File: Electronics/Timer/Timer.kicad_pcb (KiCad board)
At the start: 2 copper layers, 120 x 46 mm, 21 parts, among them J1 RJ12-UNSHLD, U1 74HC165, U2 MIC5504-3.3YM5

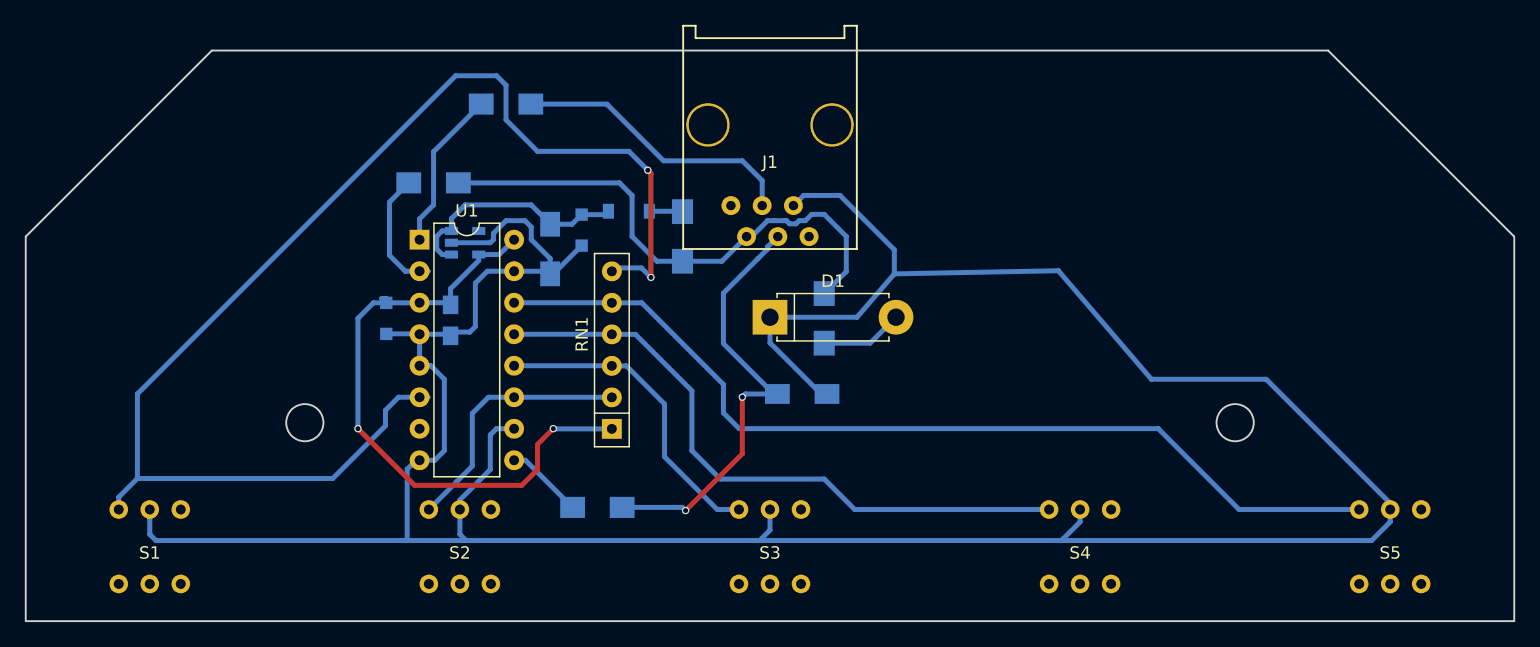
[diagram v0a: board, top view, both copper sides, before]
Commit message: Synchronized PCB with new netlist; cleaned up glitches.
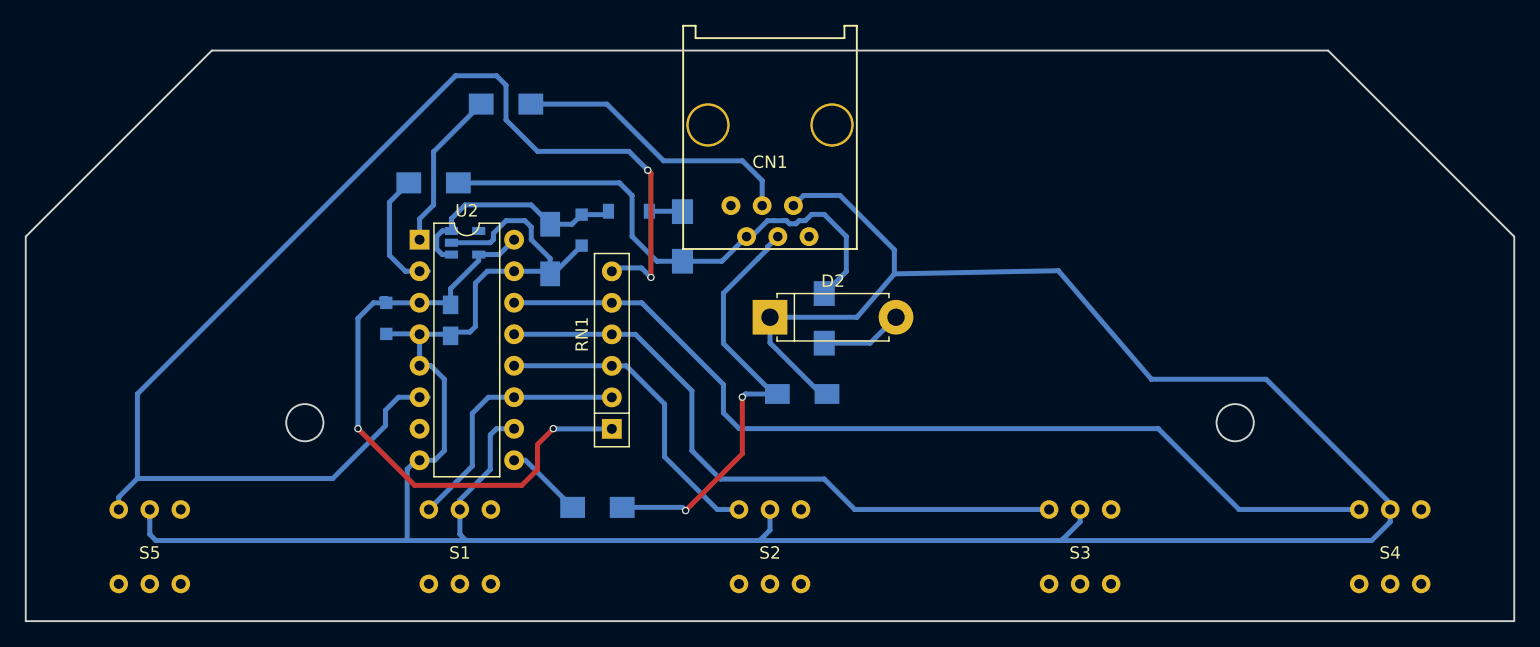
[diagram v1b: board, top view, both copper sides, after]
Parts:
- D1: renamed from D3; value D_Schottky -> BAT54
- D3: renamed from D2; value D_Zener_5V -> 5V
- D4: value D_Zener_3.3V -> 3.3V
- RN1: value R_Network05 -> 5x 47k
- turned C2 to 90 degrees
- turned R4 to 0 degrees
- renumbered C2 to C1, C1 to C2, J1 to CN1, D1 to D2, R2 to R1, R1 to R2, R5 to R3, R3 to R5, S2 to S1, S3 to S2, S4 to S3, S5 to S4, S1 to S5, U2 to U1, U1 to U2
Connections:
- net /5V-In renamed +5V
- net /PWR-CLK-IN renamed Net-(CN1-Pad2)
- net /Q-Out renamed Net-(C3-Pad1)
- C2 pad 1: +3V3 -> GND
- C2 pad 2: GND -> +3V3
- CN1 pad 1: (no net) -> Net-(CN1-Pad1)
- CN1 pad 3: Net-(J1-Pad3) -> Net-(CN1-Pad3)
- CN1 pad 6: (no net) -> Net-(CN1-Pad6)
- R4 pad 1: Net-(J1-Pad3) -> /~LOAD~
- R4 pad 2: /LOAD -> Net-(CN1-Pad3)
- S1 pad 3: (no net) -> Net-(S1-Pad3)
- S1 pad 4: (no net) -> Net-(S1-Pad4)
- S1 pad 5: (no net) -> Net-(S1-Pad5)
- S1 pad 6: (no net) -> Net-(S1-Pad6)
- S2 pad 3: (no net) -> Net-(S2-Pad3)
- S2 pad 4: (no net) -> Net-(S2-Pad4)
- S2 pad 5: (no net) -> Net-(S2-Pad5)
- S2 pad 6: (no net) -> Net-(S2-Pad6)
- S3 pad 3: (no net) -> Net-(S3-Pad3)
- S3 pad 4: (no net) -> Net-(S3-Pad4)
- S3 pad 5: (no net) -> Net-(S3-Pad5)
- S3 pad 6: (no net) -> Net-(S3-Pad6)
- S4 pad 3: (no net) -> Net-(S4-Pad3)
- S4 pad 4: (no net) -> Net-(S4-Pad4)
- S4 pad 5: (no net) -> Net-(S4-Pad5)
- S4 pad 6: (no net) -> Net-(S4-Pad6)
- S5 pad 3: (no net) -> Net-(S5-Pad3)
- S5 pad 4: (no net) -> Net-(S5-Pad4)
- S5 pad 5: (no net) -> Net-(S5-Pad5)
- S5 pad 6: (no net) -> Net-(S5-Pad6)
- U1 pad 4: (no net) -> Net-(U1-Pad4)
- U2 pad 1: /LOAD -> /~LOAD~
- U2 pad 7: (no net) -> Net-(U2-Pad7)
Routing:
- net Net-(J1-Pad3): track 23.3 -> 0.00 mm
- net Net-(CN1-Pad3): track 0.00 -> 23.3 mm
- net /~LOAD~: track 0.00 -> 13.1 mm
- net /LOAD: track 13.1 -> 0.00 mm

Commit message: Timer: Rerouted to eliminate jumpers, at the cost of a few 1206's with two traces underneath.
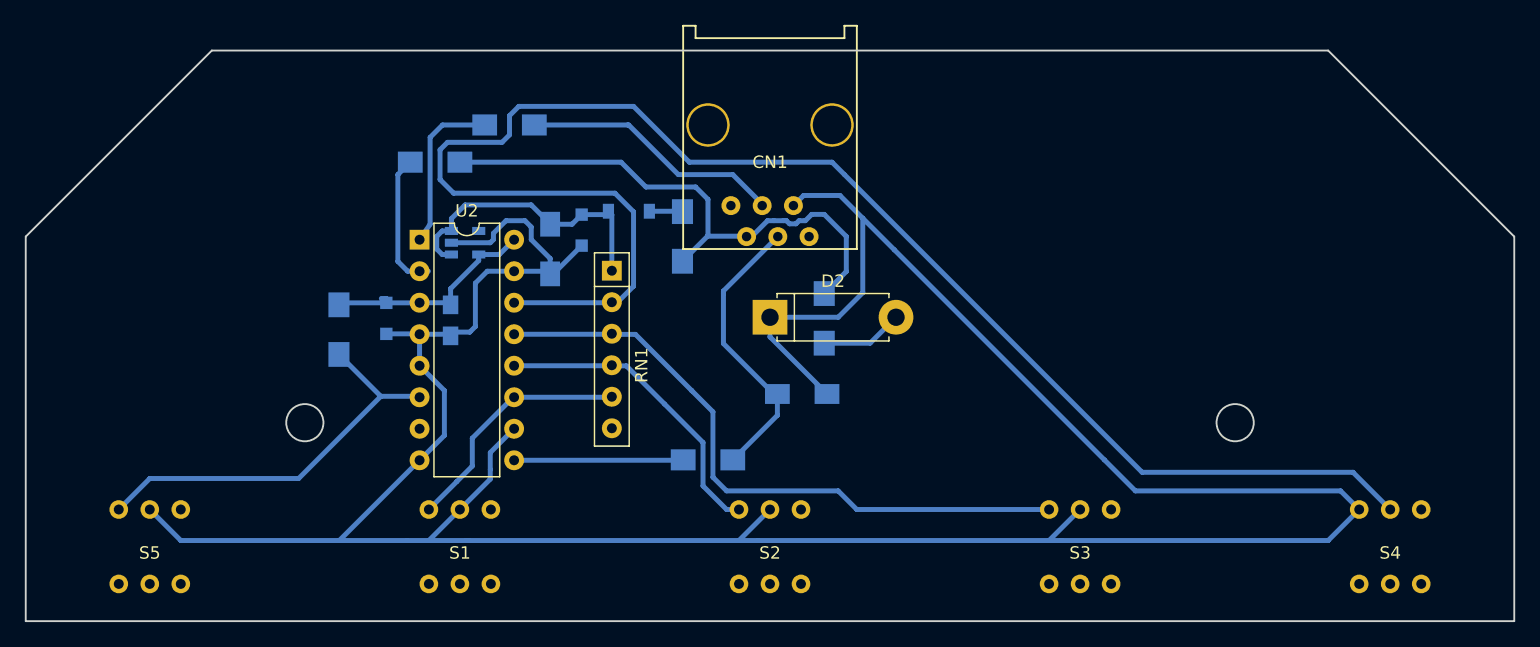
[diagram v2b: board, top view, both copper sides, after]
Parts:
- added R6: 470, Resistors_SMD:R_1206_HandSoldering, B.Cu at (65.2, 82.5)
- moved RN1 12.8 mm to (87.2, 77.8), turned to 270 degrees
- moved R5 9.70 mm to (95.0, 93.0)
- moved R4 1.71 mm to (79.0, 66.0)
- moved R3 1.67 mm to (73.0, 69.0)
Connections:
- RN1 pad 1: +3V3 -> +5V
- S1 pad 1: Net-(RN1-Pad2) -> Net-(RN1-Pad5)
- S2 pad 1: Net-(RN1-Pad3) -> Net-(RN1-Pad4)
- S3 pad 1: Net-(RN1-Pad4) -> Net-(RN1-Pad3)
- S4 pad 1: Net-(RN1-Pad5) -> GND
- S4 pad 2: GND -> Net-(RN1-Pad2)
- S5 pad 1: Net-(RN1-Pad6) -> Net-(R6-Pad2)
- U2 pad 11: Net-(RN1-Pad2) -> Net-(RN1-Pad5)
- U2 pad 12: Net-(RN1-Pad3) -> Net-(RN1-Pad4)
- U2 pad 13: Net-(RN1-Pad4) -> Net-(RN1-Pad3)
- U2 pad 14: Net-(RN1-Pad5) -> Net-(RN1-Pad2)
- U2 pad 6: Net-(RN1-Pad6) -> Net-(R6-Pad2)
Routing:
- net Net-(RN1-Pad2): track 21.0 -> 128.2 mm
- net Net-(RN1-Pad6): track 105.7 -> 0.00 mm, vias 2 -> 0
- net Net-(RN1-Pad5): track 76.4 -> 19.8 mm
- net +3V3: track 52.2 -> 19.0 mm, vias 2 -> 0
- net Net-(R6-Pad2): track 0.00 -> 32.8 mm
- net Net-(RN1-Pad4): track 52.4 -> 25.0 mm
- net Net-(RN1-Pad3): track 25.4 -> 52.7 mm
- net Net-(C3-Pad1): track 35.8 -> 23.5 mm, vias 2 -> 0
- net /Q: track 6.29 -> 13.6 mm
- net +5V: track 19.0 -> 23.9 mm
- net GND: track 257.9 -> 253.1 mm
- net Net-(CN1-Pad3): track 23.3 -> 21.3 mm
- net Net-(CN1-Pad2): track 43.7 -> 45.3 mm
- net /CLK: track 10.2 -> 11.2 mm

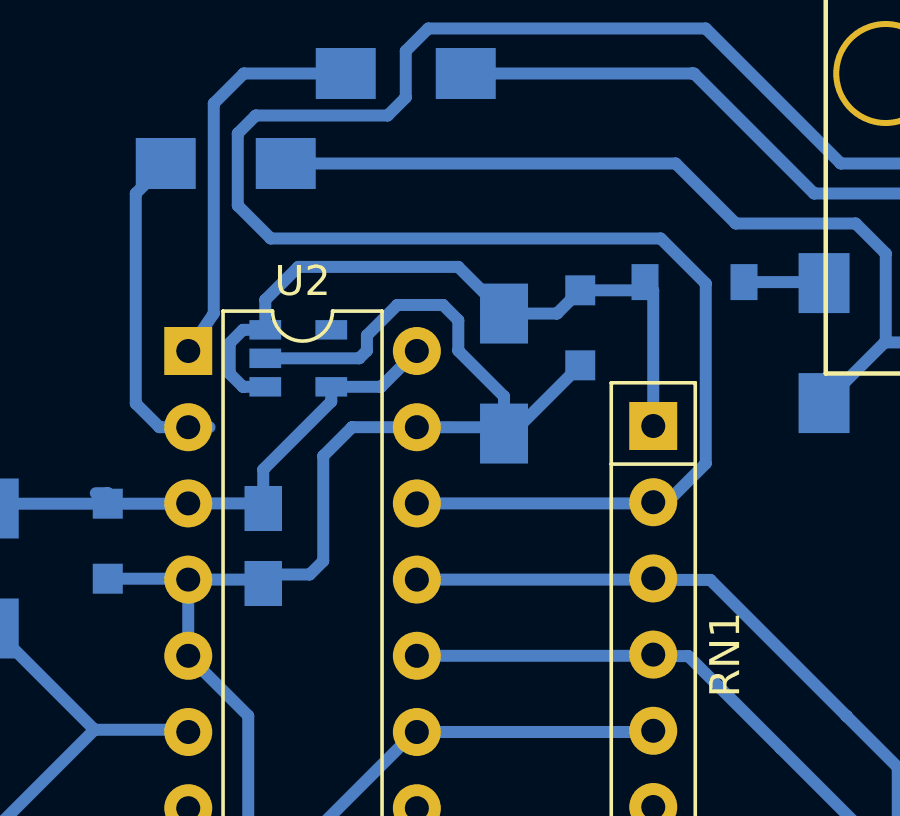
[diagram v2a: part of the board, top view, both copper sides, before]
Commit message: Timer: Increased C2 to 1 uF (per datasheet for U1 stability); brought RN1 back to 3.3 V instead of 5 V.
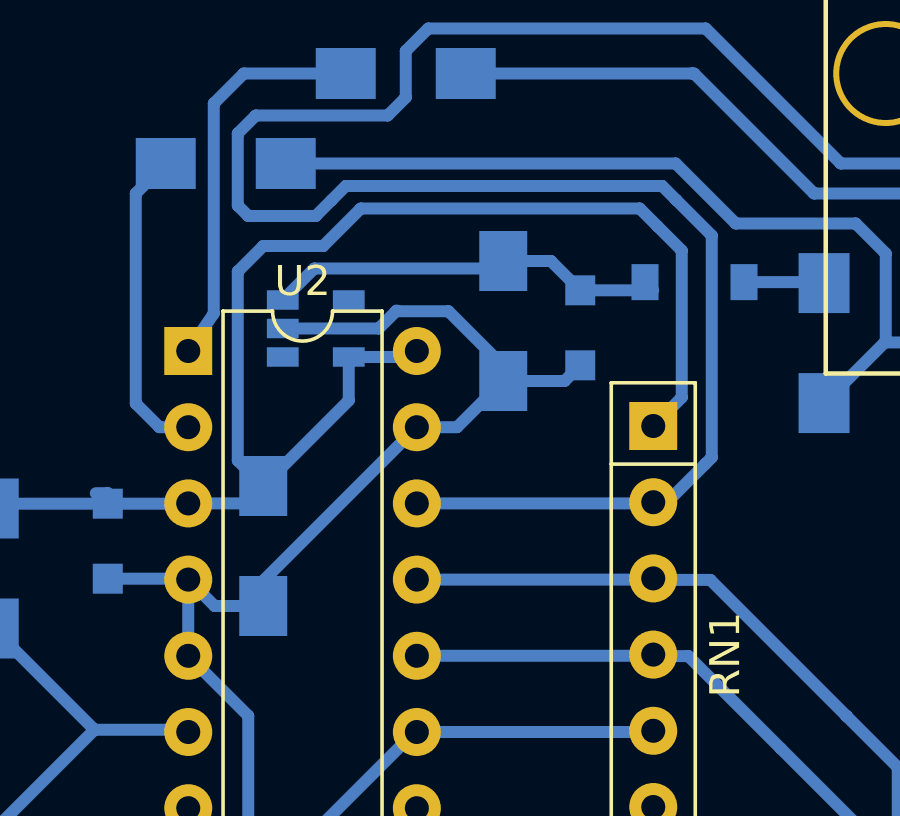
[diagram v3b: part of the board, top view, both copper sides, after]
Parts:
- C2: value 10nF -> 1uF; footprint Capacitors_SMD:C_0805_HandSoldering -> Capacitors_SMD:C_1206_HandSoldering
- moved C1 1.75 mm to (82.2, 74.2)
- moved U1 1.15 mm to (76.0, 74.5)
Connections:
- RN1 pad 1: +5V -> +3V3
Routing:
- net +3V3: track 19.0 -> 48.9 mm
- net +5V: track 23.9 -> 13.5 mm
- net GND: track 253.1 -> 248.4 mm
- net Net-(RN1-Pad2): track 128.2 -> 130.2 mm
- net /CLK: track 11.2 -> 10.5 mm

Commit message: Updated Timer project to kicad 5
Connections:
- CN1 pad 1: Net-(CN1-Pad1) -> (no net)
- CN1 pad 6: Net-(CN1-Pad6) -> (no net)
- RN1 pad 6: Net-(RN1-Pad6) -> (no net)
- S1 pad 3: Net-(S1-Pad3) -> (no net)
- S1 pad 4: Net-(S1-Pad4) -> (no net)
- S1 pad 5: Net-(S1-Pad5) -> (no net)
- S1 pad 6: Net-(S1-Pad6) -> (no net)
- S2 pad 3: Net-(S2-Pad3) -> (no net)
- S2 pad 4: Net-(S2-Pad4) -> (no net)
- S2 pad 5: Net-(S2-Pad5) -> (no net)
- S2 pad 6: Net-(S2-Pad6) -> (no net)
- S3 pad 3: Net-(S3-Pad3) -> (no net)
- S3 pad 4: Net-(S3-Pad4) -> (no net)
- S3 pad 5: Net-(S3-Pad5) -> (no net)
- S3 pad 6: Net-(S3-Pad6) -> (no net)
- S4 pad 3: Net-(S4-Pad3) -> (no net)
- S4 pad 4: Net-(S4-Pad4) -> (no net)
- S4 pad 5: Net-(S4-Pad5) -> (no net)
- S4 pad 6: Net-(S4-Pad6) -> (no net)
- S5 pad 3: Net-(S5-Pad3) -> (no net)
- S5 pad 4: Net-(S5-Pad4) -> (no net)
- S5 pad 5: Net-(S5-Pad5) -> (no net)
- S5 pad 6: Net-(S5-Pad6) -> (no net)
- U1 pad 4: Net-(U1-Pad4) -> (no net)
- U2 pad 7: Net-(U2-Pad7) -> (no net)

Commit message: Updated Timer Manufacturing files
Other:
- board size 120 x 46 mm -> 110 x 46 mm
